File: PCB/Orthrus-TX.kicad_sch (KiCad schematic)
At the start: 154 parts, among them J1 HRO-TYPE-C-31-M-13x, U1 AO3407A, U2 SRV05-4, U3 SRV05-4, U4 SRV05-4, U5 SRV05-4, U6 SRV05-4, U7 SRV05-4, U8 SRV05-4

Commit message: pcb update
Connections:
- net BATT_IN: now also U1.2 (S); no longer U1.1 (G)
- net at R57.1: now also U1.1 (G); no longer U1.2 (S)
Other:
- moved on the sheet: R57
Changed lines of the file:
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@@
 	(wire
 		(pts
+			(xy 48.26 34.29) (xy 52.07 34.29)
+		)
+		(stroke
+			(width 0)
+			(type default)
+		)
+	)
+	(wire
+		(pts
 			(xy 180.34 46.99) (xy 170.18 46.99)
 		)
@@
 	(wire
 		(pts
-			(xy 43.18 34.29) (xy 52.07 34.29)
-		)
-		(stroke
-			(width 0)
-			(type default)
-		)
-	)
-	(wire
-		(pts
 			(xy 452.12 29.21) (xy 452.12 25.4)
 		)
@@
 	(wire
 		(pts
-			(xy 92.71 36.83) (xy 96.52 36.83)
-		)
-		(stroke
-			(width 0)
-			(type default)
-		)
-	)
-	(wire
-		(pts
 			(xy 138.43 66.04) (xy 147.32 66.04)
 		)
@@
 	(wire
 		(pts
+			(xy 92.71 36.83) (xy 101.6 36.83)
+		)
+		(stroke
+			(width 0)
+			(type default)
+		)
+	)
+	(wire
+		(pts
 			(xy 502.92 20.32) (xy 509.27 20.32)
 		)
@@
 	(wire
 		(pts
-			(xy 90.17 44.45) (xy 96.52 44.45)
+			(xy 41.91 41.91) (xy 48.26 41.91)
 		)
 		(stroke
@@
 		)
 	)
-	(label "BATT_IN"
-		(at 43.18 34.29 0)
-		(effects
-			(font
-				(size 1.27 1.27)
-			)
-			(justify left bottom)
-		)
-	)
 	(label "PG13"
 		(at 128.27 350.52 0)
@@
 		)
 	)
+	(label "BATT_IN"
+		(at 93.98 36.83 0)
+		(effects
+			(font
+				(size 1.27 1.27)
+			)
+			(justify left bottom)
+		)
+	)
 	(label "PD0"
 		(at 259.08 119.38 0)
@@
 	(symbol
 		(lib_id "Device:R_US")
-		(at 96.52 40.64 0)
+		(at 48.26 38.1 0)
 		(unit 1)
 		(body_style 1)
@@
 		(dnp no)
 		(property "Reference" "R57"
-			(at 94.234 42.418 90)
+			(at 45.974 39.878 90)
 			(show_name no)
 			(do_not_autoplace no)
@@
 		)
 		(property "Value" "100kΩ"
-			(at 98.552 43.688 90)
+			(at 50.292 41.148 90)
 			(show_name no)
 			(do_not_autoplace no)
@@
 		)
 		(property "Footprint" "Resistor_SMD:R_0603_1608Metric"
-			(at 97.536 40.894 90)
+			(at 49.276 38.354 90)
 			(hide yes)
 			(show_name no)
@@
 		)
 		(property "Datasheet" ""
-			(at 96.52 40.64 0)
+			(at 48.26 38.1 0)
 			(hide yes)
 			(show_name no)
@@
 		)
 		(property "Description" "Resistor, US symbol"
-			(at 96.52 40.64 0)
+			(at 48.26 38.1 0)
 			(hide yes)
 			(show_name no)
@@
 		)
 		(property "LCSC" "C122538"
-			(at 96.52 40.64 0)
+			(at 48.26 38.1 0)
 			(hide yes)
 			(show_name no)
@@
 	(symbol
 		(lib_id "power:GND")
-		(at 90.17 44.45 0)
+		(at 41.91 41.91 0)
 		(unit 1)
 		(body_style 1)
@@
 		(dnp no)
 		(property "Reference" "#PWR080"
-			(at 90.17 50.8 0)
+			(at 41.91 48.26 0)
 			(hide yes)
 			(show_name no)
@@
 		)
 		(property "Value" "GND"
-			(at 90.17 48.006 0)
+			(at 41.91 45.466 0)
 			(show_name no)
 			(do_not_autoplace no)
@@
 		)
 		(property "Footprint" ""
-			(at 90.17 44.45 0)
+			(at 41.91 41.91 0)
 			(hide yes)
 			(show_name no)
@@
 		)
 		(property "Datasheet" ""
-			(at 90.17 44.45 0)
+			(at 41.91 41.91 0)
 			(hide yes)
 			(show_name no)
@@
 		)
 		(property "Description" "Power symbol creates a global label with name \"GND\" , ground"
-			(at 90.17 44.45 0)
+			(at 41.91 41.91 0)
 			(hide yes)
 			(show_name no)

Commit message: pcb update
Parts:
- removed FL1: 0603USB-601, Inductor_SMD:L_CommonModeChoke_Coilcraft_0603USB, symbol Filter:0603USB-601
- added C63, C64: 2.2µF, Capacitor_SMD:C_0603_1608Metric, symbol Device:C_Small_US
- added L2: DLW21SN900SQ2L, IND_DLW21S_0805_MUR, symbol IND_DLW21S_0805_MUR:DLW21SN900SQ2L
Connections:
- net GND: now also C63.1, C64.2
- net USB_N: now also L2.1
- net USB_N_OUT: now also L2.2
- net USB_P: now also L2.4
- net USB_P_OUT: now also L2.3
- net VCAP: now also C63.2, C64.1

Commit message: pcb update
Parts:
- C23, C24: value 33pF -> 12pF; LCSC C472790 -> C882527
- L2: LCSC (none) -> C97856
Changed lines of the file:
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@@
 			)
 		)
-		(property "Value" "33pF"
+		(property "Value" "12pF"
 			(at 501.65 315.0869 0)
 			(show_name no)
@@
 			)
 		)
-		(property "LCSC" "C472790"
+		(property "LCSC" "C882527"
 			(at 499.11 313.69 0)
 			(hide yes)
@@
 			)
 		)
+		(property "LCSC" "C97856"
+			(at 207.01 201.93 0)
+			(hide yes)
+			(show_name no)
+			(do_not_autoplace no)
+			(effects
+				(font
+					(size 1.27 1.27)
+				)
+			)
+		)
 		(pin "2"
 		)
@@
 			)
 		)
-		(property "Value" "33pF"
+		(property "Value" "12pF"
 			(at 417.83 293.4969 0)
 			(show_name no)
@@
 			)
 		)
-		(property "LCSC" "C472790"
+		(property "LCSC" "C882527"
 			(at 415.29 292.1 0)
 			(hide yes)

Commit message: pcb update
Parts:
- added L3: BLM18AG102SN1D, BLM18_MUR, symbol BLM18_MUR:BLM18AG102SN1D
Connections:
- net LD2_3.3v: now also L3.2; no longer C45.2, C46.2, STM32H745ZIT6.36 (VDDA)
- new net VDDA: C45.2, C46.2, L3.1, STM32H745ZIT6.36 (VDDA)
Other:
- moved on the sheet: C45, C46

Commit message: pcb update
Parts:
- L2: footprint IND_DLW21S_0805_MUR -> Custom-Library:IND_DLW21S_0805_MUR
- L3: footprint BLM18_MUR -> Custom-Library:BLM18_MUR; LCSC (none) -> C85824
- U1: footprint SOT-23-3L_AOS -> Custom-Library:SOT-23-3L_AOS
- U2, U3, U4, U5, U6, U7, U8: footprint Package_TO_SOT_SMD:SOT-23-6 -> Custom-Library:SOT-23-6
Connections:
- net GND: now also ELRS_1.5, ELRS_1.8, ELRS_2.5, ELRS_2.8; no longer ELRS_1.4, ELRS_1.6, ELRS_2.4, ELRS_2.6
- net PB5: now also ELRS_2.6, U6.6 (IO4); no longer ELRS_2.7, U6.4 (IO3)
- net PB8: now also ELRS_2.7, U6.4 (IO3); no longer ELRS_2.8, U6.6 (IO4)
- net PD10: now also ELRS_1.6, U5.6 (IO4); no longer ELRS_1.7, U5.4 (IO3)
- net PD11: now also ELRS_1.7, U5.4 (IO3); no longer ELRS_1.8, U5.6 (IO4)
- net PD8: now also U5.3 (IO2); no longer U5.1 (IO1)
- net PD9: now also ELRS_1.4, U5.1 (IO1); no longer ELRS_1.5, U5.3 (IO2)
- net PE7: now also ELRS_2.4; no longer ELRS_2.5
- net USB_N_OUT renamed USB_D_N
- net USB_P_OUT renamed USB_D_P

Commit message: pcb update
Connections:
- net USB_N: now also U2.1 (IO1); no longer U2.3 (IO2)
- net USB_P: now also U2.3 (IO2); no longer U2.1 (IO1)
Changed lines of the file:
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@@
 	(wire
 		(pts
+			(xy 259.08 236.22) (xy 270.51 236.22)
+		)
+		(stroke
+			(width 0)
+			(type default)
+		)
+	)
+	(wire
+		(pts
 			(xy 433.07 189.23) (xy 422.91 189.23)
 		)
@@
 	(wire
 		(pts
-			(xy 254 236.22) (xy 270.51 236.22)
+			(xy 228.6 279.4) (xy 237.49 279.4)
 		)
 		(stroke
@@
 	(wire
 		(pts
-			(xy 228.6 279.4) (xy 237.49 279.4)
+			(xy 36.83 293.37) (xy 36.83 300.99)
 		)
 		(stroke
@@
 	(wire
 		(pts
-			(xy 36.83 293.37) (xy 36.83 300.99)
+			(xy 355.6 172.72) (xy 364.49 172.72)
 		)
 		(stroke
@@
 	(wire
 		(pts
-			(xy 355.6 172.72) (xy 364.49 172.72)
+			(xy 259.08 240.03) (xy 265.43 240.03)
 		)
 		(stroke
@@
 	(wire
 		(pts
-			(xy 254 240.03) (xy 265.43 240.03)
-		)
-		(stroke
-			(width 0)
-			(type default)
-		)
-	)
-	(wire
-		(pts
 			(xy 214.63 292.1) (xy 217.17 292.1)
 		)
@@
 	(wire
 		(pts
+			(xy 270.51 240.03) (xy 270.51 236.22)
+		)
+		(stroke
+			(width 0)
+			(type default)
+		)
+	)
+	(wire
+		(pts
 			(xy 53.34 318.77) (xy 71.12 318.77)
 		)
@@
 	(wire
 		(pts
-			(xy 270.51 240.03) (xy 270.51 236.22)
-		)
-		(stroke
-			(width 0)
-			(type default)
-		)
-	)
-	(wire
-		(pts
 			(xy 406.4 299.72) (xy 415.29 299.72)
 		)
@@
 		)
 	)
-	(label "USB_N"
-		(at 254 240.03 0)
-		(effects
-			(font
-				(size 1.27 1.27)
-			)
-			(justify left bottom)
-		)
-	)
 	(label "PF14"
 		(at 426.72 133.35 0)
@@
 		)
 	)
+	(label "USB_P"
+		(at 259.08 240.03 0)
+		(effects
+			(font
+				(size 1.27 1.27)
+			)
+			(justify left bottom)
+		)
+	)
 	(label "LD2_3.3v"
 		(at 166.37 67.31 0)
@@
 		)
 	)
-	(label "USB_P"
-		(at 254 236.22 0)
-		(effects
-			(font
-				(size 1.27 1.27)
-			)
-			(justify left bottom)
-		)
-	)
 	(label "PA5"
 		(at 520.7 72.39 0)
@@
 		(effects
 			(font
+				(size 1.27 1.27)
+			)
+			(justify left bottom)
+		)
+	)
+	(label "USB_N"
+		(at 259.08 236.22 0)
+		(effects
+			(font

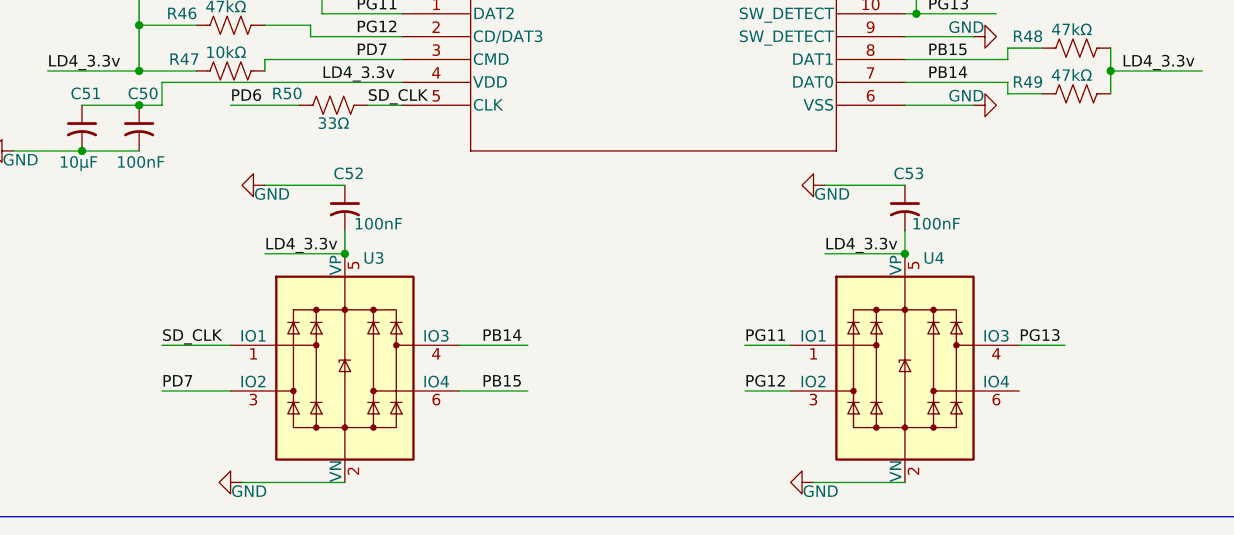
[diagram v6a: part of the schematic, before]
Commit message: sd card routing update
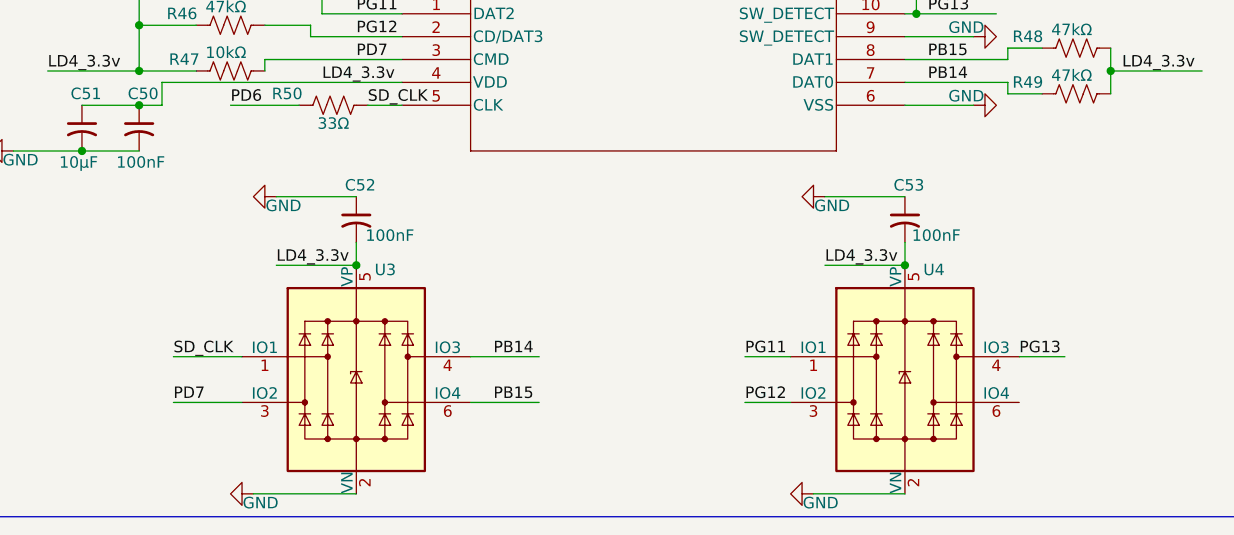
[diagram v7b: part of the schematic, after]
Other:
- moved on the sheet: C52, C53, U3, U4

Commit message: pcb update
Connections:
- net PB14: now also U3.6 (IO4); no longer U3.4 (IO3)
- net PB15: now also U3.4 (IO3); no longer U3.6 (IO4)
- net PD7: now also U3.1 (IO1); no longer U3.3 (IO2)
- net PG13: now also U4.6 (IO4); no longer U4.4 (IO3)
- net SD_CLK: now also U3.3 (IO2); no longer U3.1 (IO1)
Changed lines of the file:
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@@
 	(wire
 		(pts
+			(xy 138.43 393.7) (xy 143.51 393.7)
+		)
+		(stroke
+			(width 0)
+			(type default)
+		)
+	)
+	(wire
+		(pts
 			(xy 499.11 307.34) (xy 499.11 311.15)
 		)
@@
 	(wire
 		(pts
-			(xy 138.43 388.62) (xy 143.51 388.62)
-		)
-		(stroke
-			(width 0)
-			(type default)
-		)
-	)
-	(wire
-		(pts
 			(xy 519.43 90.17) (xy 524.51 90.17)
 		)
@@
 		)
 	)
-	(label "PD7"
+	(label "SD_CLK"
 		(at 44.45 393.7 0)
 		(effects
@@
 		)
 	)
+	(label "PG13"
+		(at 138.43 393.7 0)
+		(effects
+			(font
+				(size 1.27 1.27)
+			)
+			(justify left bottom)
+		)
+	)
 	(label "PD3"
 		(at 259.08 127 0)
@@
 		)
 	)
-	(label "PG13"
-		(at 138.43 388.62 0)
-		(effects
-			(font
-				(size 1.27 1.27)
-			)
-			(justify left bottom)
-		)
-	)
 	(label "PD3"
 		(at 520.7 196.85 0)
@@
 		)
 	)
-	(label "SD_CLK"
+	(label "PD7"
 		(at 44.45 388.62 0)
 		(effects
@@
 		)
 	)
-	(label "PB15"
+	(label "PB14"
 		(at 80.01 393.7 0)
 		(effects
@@
 		)
 	)
-	(label "PB14"
+	(label "PB15"
 		(at 80.01 388.62 0)
 		(effects
@@
 		)
 	)
-	(group ""
-		(members "3a4bba30-68ad-46cf-b188-abe0e7af837b" "3b7a38aa-58b4-4eb6-8d10-6acbec32d3ce"
-			"51e80c94-7037-457c-b10a-5495ca2b8dbd" "6037b47f-664c-4e89-8579-48cf77599206"
-			"6263babc-a363-47a5-961e-a5a0c4347a6e" "6b9daf19-8d74-4d45-be00-2d8efd07b7a3"
-			"739449ee-12a1-45e4-9072-e129b93ac183" "75360525-dc64-474c-87bd-96689593aaa5"
-			"7756d31a-f973-4c10-87d4-28c3adaf912e" "78380891-e884-4437-a204-0a78c55fa504"
-			"9a82ac1a-4a5e-4b2e-ba1a-d0591275b92f" "9cc51036-9eb1-4dc6-9867-c666b8dcd35e"
-			"bda3ad92-2123-4414-8025-8430603d0307" "bfe385e4-3658-43ce-aa1b-0e2647ec1ebf"
-			"e8f48d31-0bcf-4481-9cb0-5c365c96b14e" "f557255f-f2be-4fc6-9cd6-85d8879d302d"
-		)
-	)
